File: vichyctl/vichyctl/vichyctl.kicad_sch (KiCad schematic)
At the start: 13 parts, among them J1 Conn_01x02_Pin, J2 Conn_01x03_Pin, Q1 BC549, U1 ESP32-WROOM-32

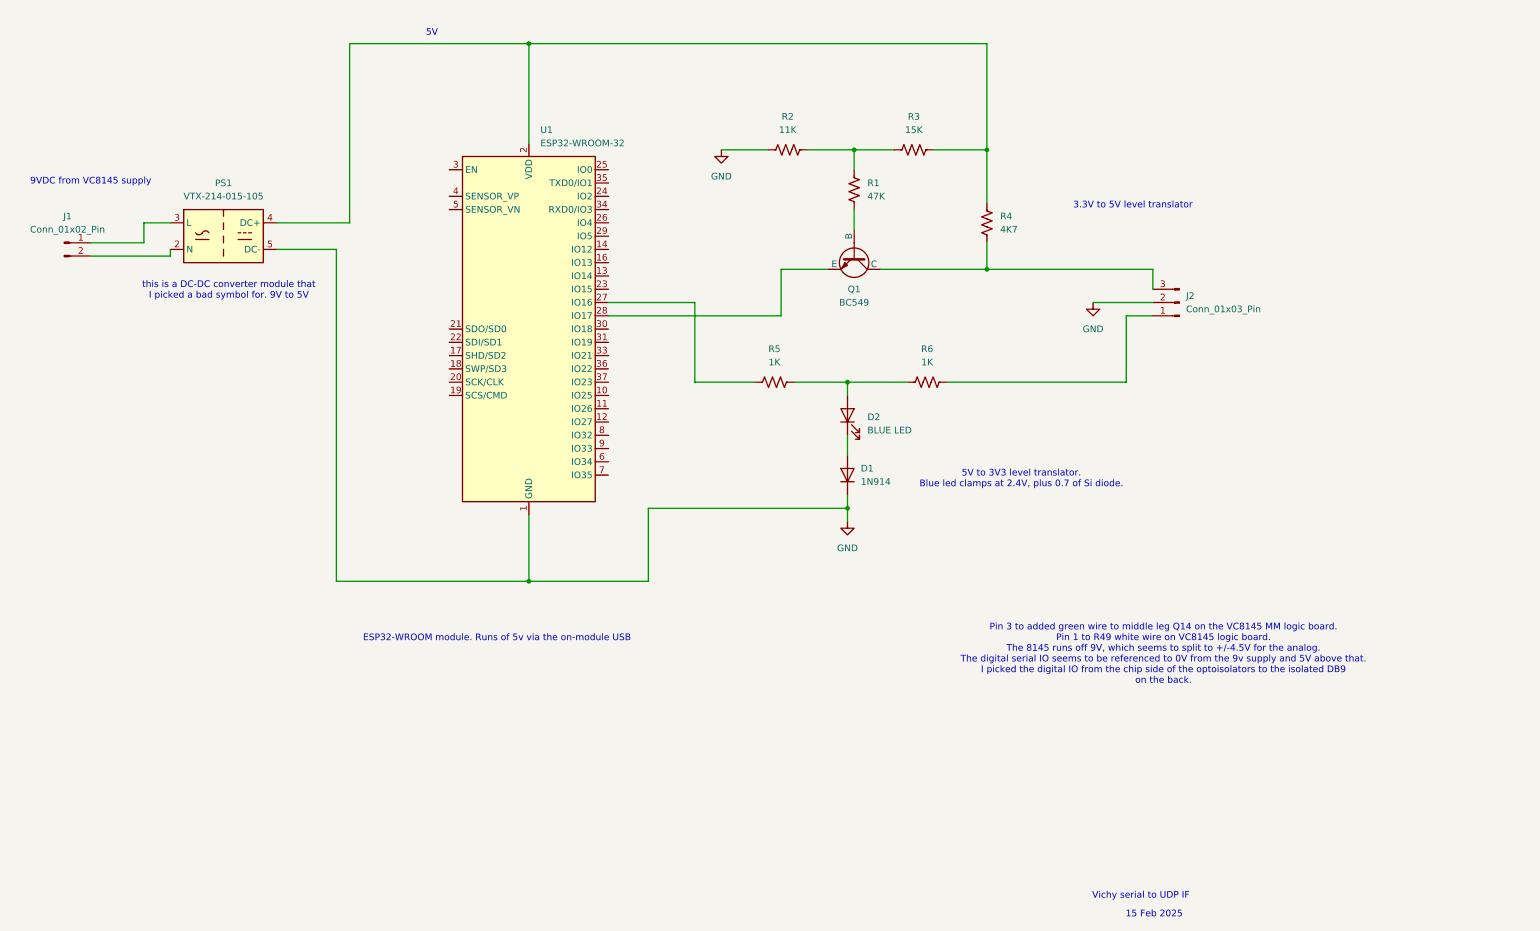
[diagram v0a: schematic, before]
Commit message: drew 4 boards, asked pcbway to make some
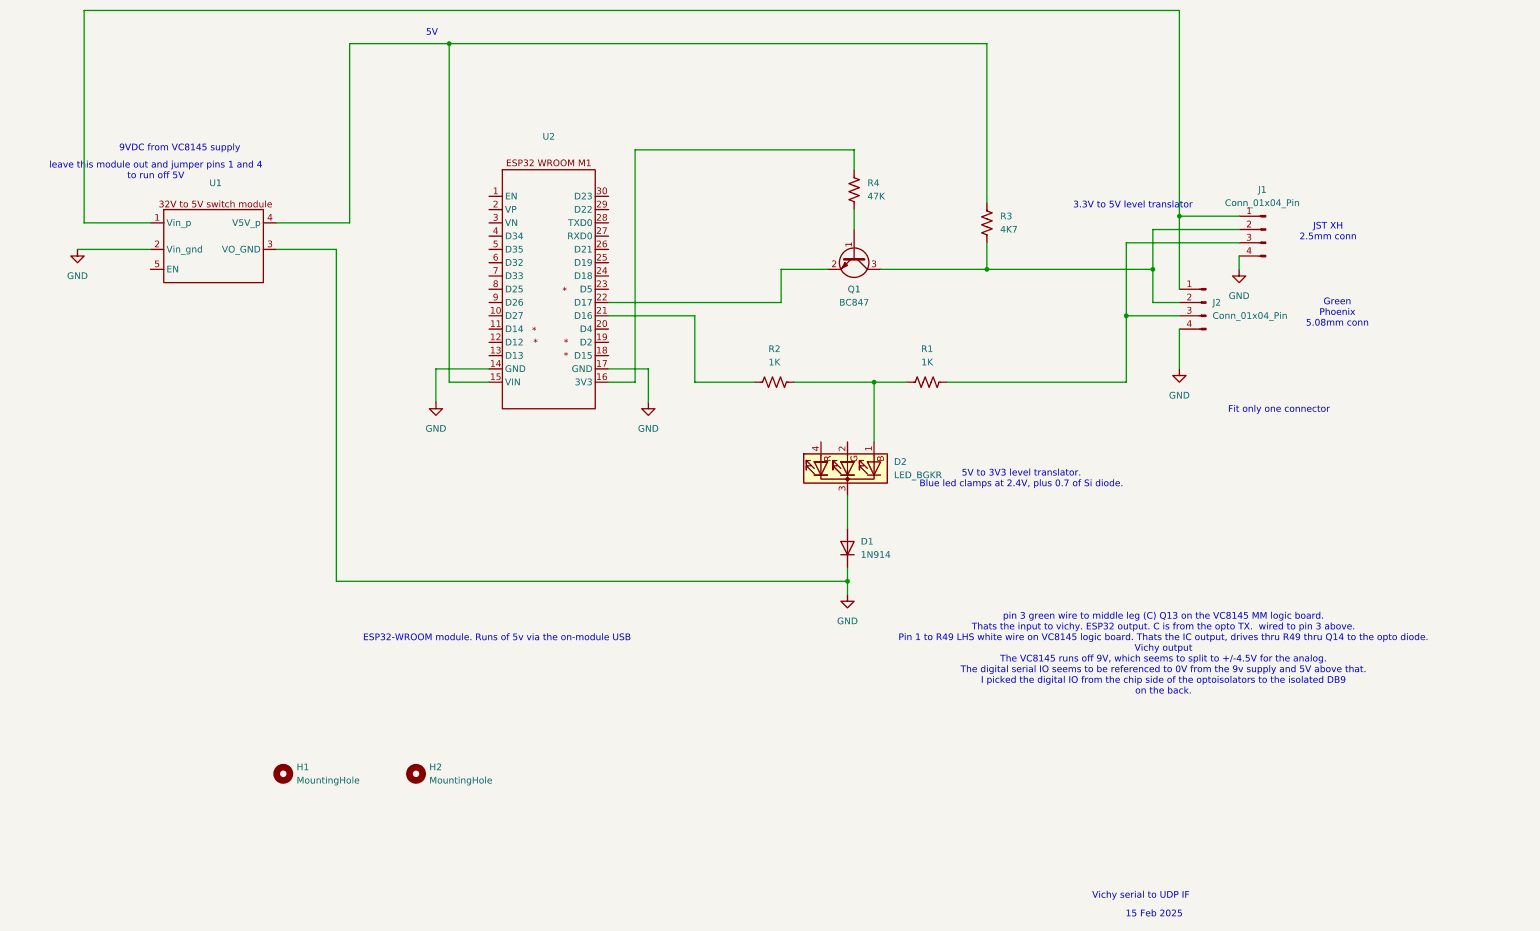
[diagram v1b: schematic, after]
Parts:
- removed D2: BLUE LED, symbol Device:LED
- removed J1: Conn_01x02_Pin, symbol Connector:Conn_01x02_Pin
- removed J2: Conn_01x03_Pin, symbol Connector:Conn_01x03_Pin
- removed PS1: VTX-214-015-105, Converter_ACDC:Converter_ACDC_Vigortronix_VTX-214-015-1xx_THT, symbol Converter_ACDC:VTX-214-015-105
- removed Q1: BC549, symbol Simulation_SPICE:NPN
- removed R2: 11K, symbol Device:R_US
- removed R3: 15K, symbol Device:R_US
- removed U1: ESP32-WROOM-32, RF_Module:ESP32-WROOM-32, symbol RF_Module:ESP32-WROOM-32
- added D2: LED_BGKR, LED_THT:LED_D5.0mm-4_RGB_Wide_Pins, symbol Device:LED_BGKR
- added H1, H2: MountingHole, MountingHole:MountingHole_3.2mm_M3_ISO7380, symbol Mechanical:MountingHole
- added J1: Conn_01x04_Pin, Connector_JST:JST_XH_B4B-XH-A_1x04_P2.50mm_Vertical, symbol Connector:Conn_01x04_Pin
- added J2: Conn_01x04_Pin, Connector_Phoenix_MC_HighVoltage:PhoenixContact_MC_1,5_4-G-5.08_1x04_P5.08mm_Horizontal, symbol Connector:Conn_01x04_Pin
- added Q1: BC847, Package_TO_SOT_SMD:SOT-23, symbol Transistor_BJT:BC847
- added U1: ~, mower_footprints:switcher_en, symbol mower:5Vsw_module
- added U2: ~, mower_footprints:ESP32_WROOM_M1, symbol mower:ESP32_wroom32_m1
- D1: footprint (none) -> Diode_SMD:D_0603_1608Metric_Pad1.05x0.95mm_HandSolder
- R1: renamed from R6; footprint (none) -> Resistor_SMD:R_0805_2012Metric_Pad1.20x1.40mm_HandSolder
- R2: renamed from R5; footprint (none) -> Resistor_SMD:R_0805_2012Metric_Pad1.20x1.40mm_HandSolder
- R3: renamed from R4; footprint (none) -> Resistor_SMD:R_0805_2012Metric_Pad1.20x1.40mm_HandSolder
- R4: renamed from R1; footprint (none) -> Resistor_SMD:R_0805_2012Metric_Pad1.20x1.40mm_HandSolder
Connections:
- net GND: now also J1.4 (Pin_4), J2.4 (Pin_4), U1.2 (Vin_gnd), U1.3 (VO_GND), U2.14 (GND), U2.17 (GND)
- net at R2.1: now also U2.21 (D16)
- net at R1.1, R2.2: now also D2.1 (BA)
- net at R1.2: now also J1.3 (Pin_3), J2.3 (Pin_3)
- net at R3.2: now also J1.2 (Pin_2), J2.2 (Pin_2), Q1.3 (C)
- net at R3.1: now also U1.4 (V5V_p), U2.15 (VIN)
- net at R4.2: now also U2.16 (3V3)
- net at R4.1: now also Q1.1 (B)
- net at D1.2 (A): now also D2.3 (K)
- new net: Q1.2 (E), U2.22 (D17)
- new net: J1.1 (Pin_1), J2.1 (Pin_1), U1.1 (Vin_p)
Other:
- note added: "Fit only one connector"
- note added: "Green Phoenix 5.08mm conn"
- note added: "JST XH 2.5mm conn"
- note added: "leave this module out and jumper pins 1 and 4 to run off 5V"
- note added: "pin 3 green wire to middle leg (C) Q13 on the VC8145 MM logic board. Thats the input to vichy. ESP32 output. C is from the opto TX. wired to pin 3 above. Pin 1 to R49 LHS white wire on VC8145 logic board. Thats the IC output, drives thru R49 thru Q14 to the opto diode. Vichy output The VC8145 runs off 9V, which seems to split to +/-4.5V for the analog. The digital serial IO seems to be referenced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"
- note removed: "Pin 3 to added green wire to middle leg Q14 on the VC8145 MM logic board. Pin 1 to R49 white wire on VC8145 logic board. The 8145 runs off 9V, which seems to split to +/-4.5V for the analog. The digital serial IO seems to be referenced to 0V from the 9v supply and 5V above that. I picked the digital IO from the chip side of the optoisolators to the isolated DB9 on the back."
- note removed: "this is a DC-DC converter module that I picked a bad symbol for. 9V to 5V"
- moved on the sheet: D1
